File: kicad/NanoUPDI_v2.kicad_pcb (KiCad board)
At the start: 2 copper layers, 10 x 22 mm, 20 parts, among them J1 Conn_01x03, SW1 VCC, U1 CH340E

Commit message: Update Kicad PCB
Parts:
- C1: value 100nF -> 100n
- SW1: value VCC -> MSK12C02
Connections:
- SW1 pad MP: GND -> (no net)
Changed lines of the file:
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@@
 		(property ki_fp_filters "TO-???* *_Diode_* *SingleDiode* D_*")
 		(sheetname "Root")
-		(sheetfile "USB-C_UPDI_programmer_v2.kicad_sch")
+		(sheetfile "NanoUPDI_v2.kicad_sch")
 		(attr smd)
 		(fp_line
@@
 		(property ki_fp_filters "R_*")
 		(sheetname "Root")
-		(sheetfile "USB-C_UPDI_programmer_v2.kicad_sch")
+		(sheetfile "NanoUPDI_v2.kicad_sch")
 		(attr smd)
 		(fp_line
@@
 			)
 		)
-		(property "Value" "100nF"
+		(property "Value" "100n"
 			(at 0 1.43 0)
 			(layer "F.Fab")
@@
 		(property ki_fp_filters "C_*")
 		(sheetname "Root")
-		(sheetfile "USB-C_UPDI_programmer_v2.kicad_sch")
+		(sheetfile "NanoUPDI_v2.kicad_sch")
 		(attr smd dnp)
 		(fp_line
@@
 		(property ki_fp_filters "R_*")
 		(sheetname "Root")
-		(sheetfile "USB-C_UPDI_programmer_v2.kicad_sch")
+		(sheetfile "NanoUPDI_v2.kicad_sch")
 		(attr smd)
 		(fp_line
@@
 		(property ki_fp_filters "R_*")
 		(sheetname "Root")
-		(sheetfile "USB-C_UPDI_programmer_v2.kicad_sch")
+		(sheetfile "NanoUPDI_v2.kicad_sch")
 		(attr smd)
 		(fp_line
@@
 		(property ki_fp_filters "SOT?23?5*")
 		(sheetname "Root")
-		(sheetfile "USB-C_UPDI_programmer_v2.kicad_sch")
+		(sheetfile "NanoUPDI_v2.kicad_sch")
 		(attr smd)
 		(fp_line
@@
 		(property ki_fp_filters "R_*")
 		(sheetname "Root")
-		(sheetfile "USB-C_UPDI_programmer_v2.kicad_sch")
+		(sheetfile "NanoUPDI_v2.kicad_sch")
 		(attr smd)
 		(fp_line
@@
 		(property ki_fp_filters "R_*")
 		(sheetname "Root")
-		(sheetfile "USB-C_UPDI_programmer_v2.kicad_sch")
+		(sheetfile "NanoUPDI_v2.kicad_sch")
 		(attr smd)
 		(fp_line
@@
 		(property ki_fp_filters "R_*")
 		(sheetname "Root")
-		(sheetfile "USB-C_UPDI_programmer_v2.kicad_sch")
+		(sheetfile "NanoUPDI_v2.kicad_sch")
 		(attr smd)
 		(fp_line
@@
 		(property ki_fp_filters "MSOP*3x3mm*P0.5mm*")
 		(sheetname "Root")
-		(sheetfile "USB-C_UPDI_programmer_v2.kicad_sch")
+		(sheetfile "NanoUPDI_v2.kicad_sch")
 		(attr smd)
 		(fp_line
@@
 		(property ki_fp_filters "C_*")
 		(sheetname "Root")
-		(sheetfile "USB-C_UPDI_programmer_v2.kicad_sch")
+		(sheetfile "NanoUPDI_v2.kicad_sch")
 		(attr smd)
 		(fp_line
@@
 		(property ki_fp_filters "C_*")
 		(sheetname "Root")
-		(sheetfile "USB-C_UPDI_programmer_v2.kicad_sch")
+		(sheetfile "NanoUPDI_v2.kicad_sch")
 		(attr smd)
 		(fp_line
@@
 		(property ki_fp_filters "LED* LED_SMD:* LED_THT:*")
 		(sheetname "Root")
-		(sheetfile "USB-C_UPDI_programmer_v2.kicad_sch")
+		(sheetfile "NanoUPDI_v2.kicad_sch")
 		(attr smd)
 		(fp_line
@@
 		(property ki_fp_filters "Connector*:*_1x??_*")
 		(sheetname "Root")
-		(sheetfile "USB-C_UPDI_programmer_v2.kicad_sch")
+		(sheetfile "NanoUPDI_v2.kicad_sch")
 		(attr through_hole)
 		(fp_line
@@
 		(property ki_fp_filters "USB*C*Receptacle*")
 		(sheetname "Root")
-		(sheetfile "USB-C_UPDI_programmer_v2.kicad_sch")
+		(sheetfile "NanoUPDI_v2.kicad_sch")
 		(attr smd)
 		(fp_line
@@
 		(property ki_fp_filters "C_*")
 		(sheetname "Root")
-		(sheetfile "USB-C_UPDI_programmer_v2.kicad_sch")
+		(sheetfile "NanoUPDI_v2.kicad_sch")
 		(attr smd)
 		(fp_line
@@
 		(property ki_fp_filters "LED* LED_SMD:* LED_THT:*")
 		(sheetname "Root")
-		(sheetfile "USB-C_UPDI_programmer_v2.kicad_sch")
+		(sheetfile "NanoUPDI_v2.kicad_sch")
 		(attr smd)
 		(fp_line
@@
 		(property ki_fp_filters "Inductor_* L_* *Ferrite*")
 		(sheetname "Root")
-		(sheetfile "USB-C_UPDI_programmer_v2.kicad_sch")
+		(sheetfile "NanoUPDI_v2.kicad_sch")
 		(attr smd)
 		(fp_line
@@
 		(property ki_fp_filters "C_*")
 		(sheetname "Root")
-		(sheetfile "USB-C_UPDI_programmer_v2.kicad_sch")
+		(sheetfile "NanoUPDI_v2.kicad_sch")
 		(attr smd)
 		(fp_line
@@
 			)
 		)
-		(property "Value" "VCC"
+		(property "Value" "MSK12C02"
 			(at 0 1 180)
 			(layer "B.SilkS")
@@
 		)
 		(sheetname "Root")
-		(sheetfile "USB-C_UPDI_programmer_v2.kicad_sch")
+		(sheetfile "NanoUPDI_v2.kicad_sch")
 		(attr smd)
 		(fp_line
@@
 			(size 0.6 1.075)
 			(layers "B.Cu" "B.Paste" "B.Mask")
-			(net 2 "GND")
 			(zone_connect 2)
 			(teardrops
@@
 			(size 0.6 1.075)
 			(layers "B.Cu" "B.Paste" "B.Mask")
-			(net 2 "GND")
 			(zone_connect 2)
 			(teardrops
@@
 			(size 0.6 1.075)
 			(layers "B.Cu" "B.Paste" "B.Mask")
-			(net 2 "GND")
 			(zone_connect 2)
 			(teardrops
@@
 			(size 0.6 1.075)
 			(layers "B.Cu" "B.Paste" "B.Mask")
-			(net 2 "GND")
 			(zone_connect 2)
 			(teardrops

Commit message: Moved R3 further down, fixed MSK12C02 mounting pads, removed "JLCJLCJLCJLC" from silkscreen, updated to v2.2 & date
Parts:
- moved R3 2.95 mm to (153.0, 93.0)
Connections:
- SW1 pad MP: (no net) -> GND
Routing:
- net /UPDI: track 7.01 -> 4.06 mm
- net /RXD: track 9.48 -> 12.4 mm
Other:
- rule pad_to_mask_clearance: 0.038 -> 0
- board text added: "v2.2 20241213"
- board text removed: "v2.1 20241121"

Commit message: Updated solder mask configuration and gerber files for better JLCPCB compatibility
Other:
- rule pad_to_mask_clearance: 0 -> 0.038
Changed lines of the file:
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@@
 			(dielectric_constraints no)
 		)
-		(pad_to_mask_clearance 0)
-		(allow_soldermask_bridges_in_footprints no)
+		(pad_to_mask_clearance 0.038)
+		(solder_mask_min_width 0.2)
+		(allow_soldermask_bridges_in_footprints yes)
 		(aux_axis_origin 146.9 98.6)
 		(grid_origin 146.9 98.6)
@@
 			(disableapertmacros no)
 			(usegerberextensions yes)
-			(usegerberattributes yes)
-			(usegerberadvancedattributes yes)
+			(usegerberattributes no)
+			(usegerberadvancedattributes no)
 			(creategerberjobfile no)
 			(dashed_line_dash_ratio 12.000000)
@@
 			(psa4output no)
 			(plotreference yes)
-			(plotvalue yes)
+			(plotvalue no)
 			(plotfptext yes)
 			(plotinvisibletext no)
@@
 			(drillshape 0)
 			(scaleselection 1)
-			(outputdirectory "Gerber-2.2/")
+			(outputdirectory "Gerber-v2.2/")
 		)
 	)

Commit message: Fix solder mask expansion
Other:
- rule solder_mask_min_width: 0.2 -> 0.1

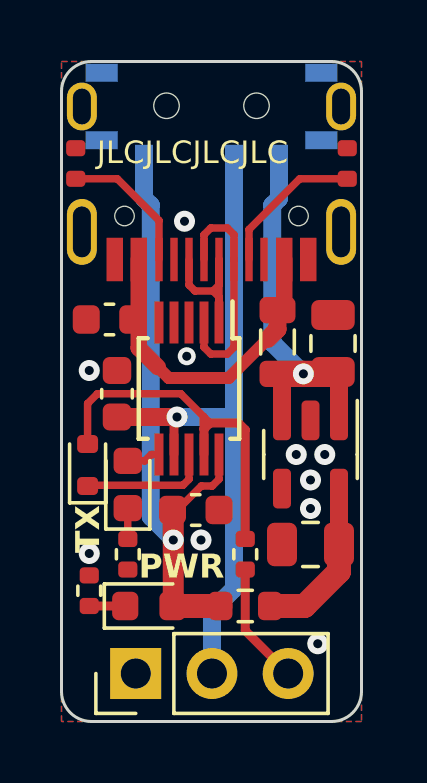
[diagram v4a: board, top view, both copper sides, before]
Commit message: Remove JLCJLCJLCJLC, tidy up Fab layer
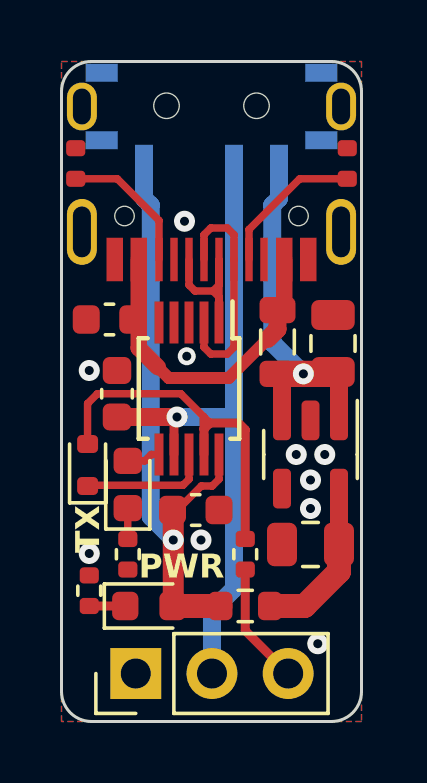
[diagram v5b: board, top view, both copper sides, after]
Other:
- board text removed: "JLCJLCJLCJLC"
